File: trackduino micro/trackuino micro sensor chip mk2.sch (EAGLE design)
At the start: 40 parts, among them IC2 74AHC1G125DBV, SW1 SPST_TACT-KMR2, U1 ATMEGA168MLF, Y1 16MHZ

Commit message: updates
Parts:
- removed LED3, LED4: (no value), adafruit:LEDCHIP-LED0805
- removed SHT15: SHT1XSMD, SparkFun-Sensors:SHT1XSMD
- added PTT, VCC: (no value), adafruit:LEDCHIP-LED0805
- added SHT21: SHT21, sht21:SHT21
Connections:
- net 3V: now also SHT21.VDD; no longer SHT15.VDD
- net GND: now also PTT.C, SHT21.VSS, VCC.C; no longer LED3.C, LED4.C, SHT15.GND
- net N$27: now also PTT.A; no longer LED4.A
- net N$8: now also VCC.A; no longer LED3.A
- net SCL: now also SHT21.SCL; no longer SHT15.SCK
- net SDA: now also SHT21.SDA; no longer SHT15.DATA
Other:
- note added: "Sensors"
- moved on the sheet: BMP180, C1, C2, C3, C4, C5, C7, C8, C9, D1, IC2, JP1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

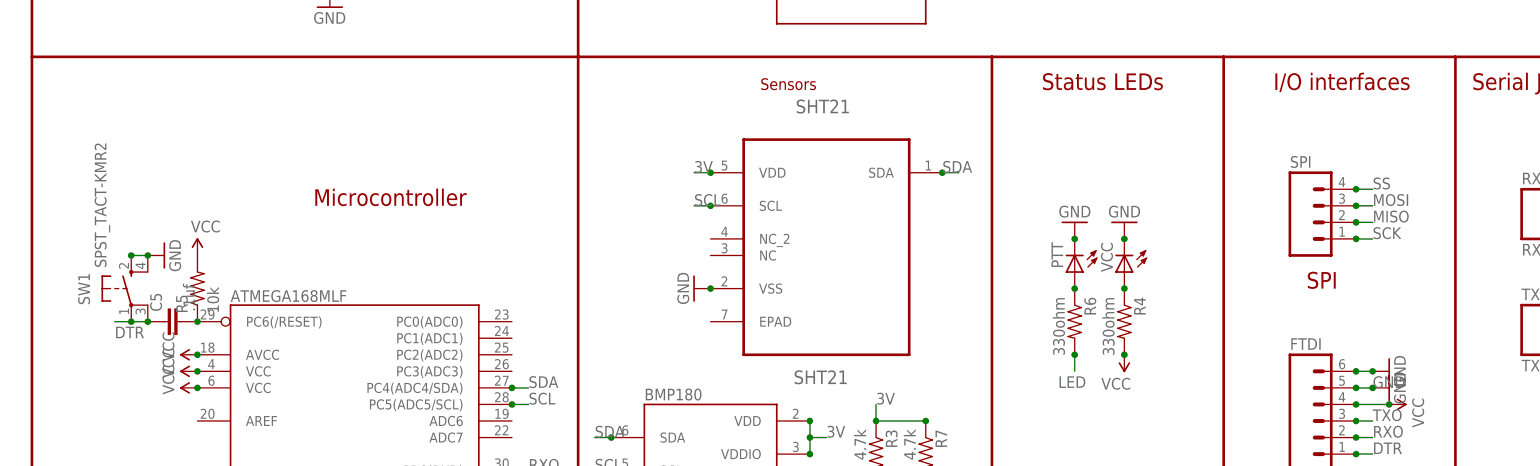
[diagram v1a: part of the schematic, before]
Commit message: added i2c breakout and fixed ftdi
added breakouts on all versions for i2c next to the spi header, replaced
IO breakout headers from .1" to 2mm to accomodate i2c.
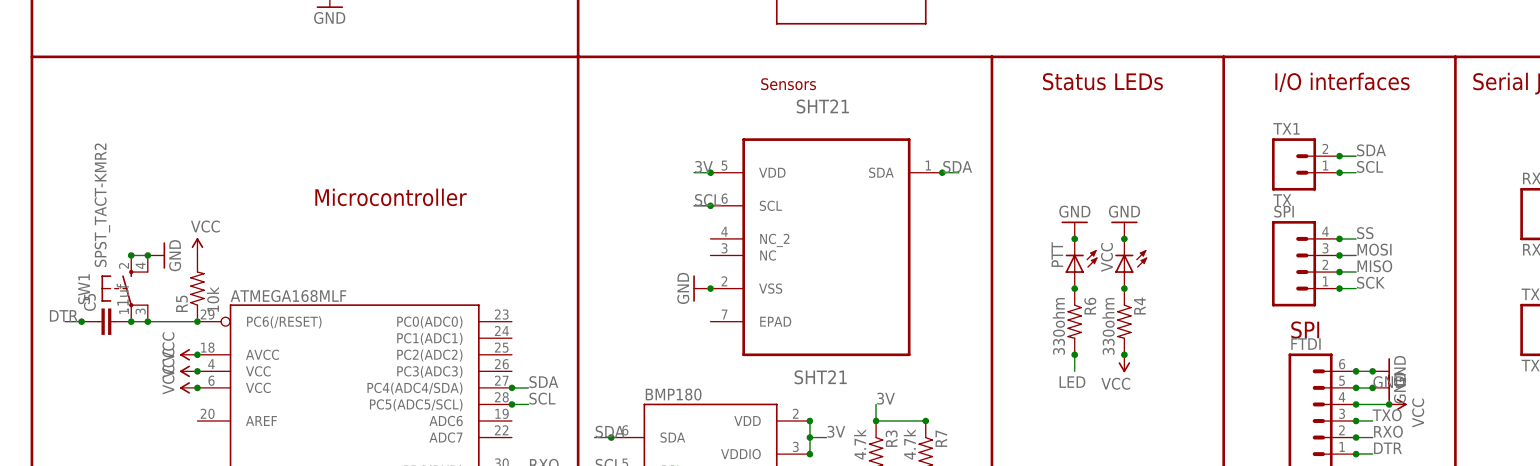
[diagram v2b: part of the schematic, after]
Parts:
- added TX1: TX, SparkFun-Connectors:M02JST-PTH-VERT
- SPI: device SparkFun-Connectors:M041X04_NO_SILK -> SparkFun-Connectors:M04JST-PTH-VERT
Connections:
- removed net N$7: C5.2, R5.1, U1.PC6(/RESET)
- new net N$17: C5.2, R5.1, SW1.P, SW1.P1, U1.PC6(/RESET)
- net DTR: no longer SW1.P, SW1.P1
- net SCL: now also TX1.1
- net SDA: now also TX1.2
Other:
- moved on the sheet: C5, SPI
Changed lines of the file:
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@@
 <part name="C5" library="SparkFun-Capacitors" deviceset="CAP" device="0805" value=".1uf"/>
 <part name="TX" library="SparkFun-Connectors" deviceset="M02" device="PTH" value="TX"/>
-<part name="SPI" library="SparkFun-Connectors" deviceset="M04" device="1X04_NO_SILK"/>
+<part name="SPI" library="SparkFun-Connectors" deviceset="M04" device="JST-PTH-VERT"/>
 <part name="GND23" library="SparkFun-Aesthetics" deviceset="GND" device=""/>
 <part name="FRAME1" library="SparkFun-Aesthetics" deviceset="FRAME-LETTER" device=""/>
@@
 <part name="SHT21" library="sht21" deviceset="SHT21" device=""/>
 <part name="U$3" library="SparkFun-RF" deviceset="ANTENNA2" device="SMD3"/>
+<part name="TX1" library="SparkFun-Connectors" deviceset="M02" device="JST-PTH-VERT" value="TX"/>
 </parts>
 <sheets>
@@
 <text x="190.5" y="104.14" size="2.54" layer="94">I/O interfaces</text>
 <text x="220.98" y="104.14" size="2.54" layer="94">Serial Jumpers</text>
-<text x="195.58" y="73.66" size="2.54" layer="94">SPI</text>
+<text x="193.04" y="66.04" size="2.54" layer="94">SPI</text>
 <text x="195.58" y="40.64" size="2.54" layer="94">FTDI</text>
 <wire x1="147.32" y1="35.56" x2="83.82" y2="35.56" width="0.1524" layer="94"/>
@@
 <instance part="R5" gate="G$1" x="25.4" y="73.66" rot="R90"/>
 <instance part="SUPPLY10" gate="G$1" x="25.4" y="78.74"/>
-<instance part="C5" gate="G$1" x="22.86" y="68.58" rot="R90"/>
+<instance part="C5" gate="G$1" x="12.7" y="68.58" rot="R90"/>
 <instance part="TX" gate="G$1" x="231.14" y="66.04"/>
-<instance part="SPI" gate="G$1" x="198.12" y="83.82"/>
+<instance part="SPI" gate="G$1" x="195.58" y="76.2"/>
 <instance part="GND23" gate="1" x="20.32" y="78.74" rot="R90"/>
 <instance part="FRAME1" gate="G$1" x="0" y="0"/>
@@
 <instance part="SHT21" gate="A" x="121.92" y="83.82"/>
 <instance part="U$3" gate="G$1" x="165.1" y="165.1" rot="R90"/>
+<instance part="TX1" gate="G$1" x="193.04" y="91.44"/>
 </instances>
 <busses>
@@
 </segment>
 <segment>
-<pinref part="SW1" gate="G$1" pin="P"/>
-<wire x1="15.24" y1="68.58" x2="17.78" y2="68.58" width="0.1524" layer="91"/>
-<pinref part="SW1" gate="G$1" pin="P1"/>
 <pinref part="C5" gate="G$1" pin="1"/>
-<junction x="17.78" y="68.58"/>
-<junction x="15.24" y="68.58"/>
-<wire x1="15.24" y1="68.58" x2="12.7" y2="68.58" width="0.1524" layer="91"/>
-<label x="12.7" y="66.04" size="1.778" layer="95"/>
+<wire x1="7.62" y1="68.58" x2="5.08" y2="68.58" width="0.1524" layer="91"/>
+<junction x="7.62" y="68.58"/>
+<label x="2.54" y="68.58" size="1.778" layer="95"/>
 </segment>
 </net>
@@
 <segment>
 <pinref part="SPI" gate="G$1" pin="2"/>
-<wire x1="203.2" y1="83.82" x2="205.74" y2="83.82" width="0.1524" layer="91"/>
-<label x="205.74" y="83.82" size="1.778" layer="95"/>
-<junction x="203.2" y="83.82"/>
+<wire x1="200.66" y1="76.2" x2="203.2" y2="76.2" width="0.1524" layer="91"/>
+<label x="203.2" y="76.2" size="1.778" layer="95"/>
+<junction x="200.66" y="76.2"/>
 </segment>
 </net>
@@
 <segment>
 <pinref part="SPI" gate="G$1" pin="3"/>
-<wire x1="203.2" y1="86.36" x2="205.74" y2="86.36" width="0.1524" layer="91"/>
-<label x="205.74" y="86.36" size="1.778" layer="95"/>
-<junction x="203.2" y="86.36"/>
+<wire x1="200.66" y1="78.74" x2="203.2" y2="78.74" width="0.1524" layer="91"/>
+<label x="203.2" y="78.74" size="1.778" layer="95"/>
+<junction x="200.66" y="78.74"/>
 </segment>
 </net>
@@
 <segment>
 <pinref part="SPI" gate="G$1" pin="1"/>
-<wire x1="203.2" y1="81.28" x2="205.74" y2="81.28" width="0.1524" layer="91"/>
-<label x="205.74" y="81.28" size="1.778" layer="95"/>
-<junction x="203.2" y="81.28"/>
+<wire x1="200.66" y1="73.66" x2="203.2" y2="73.66" width="0.1524" layer="91"/>
+<label x="203.2" y="73.66" size="1.778" layer="95"/>
+<junction x="200.66" y="73.66"/>
 </segment>
 </net>
@@
 <segment>
 <pinref part="SPI" gate="G$1" pin="4"/>
-<wire x1="203.2" y1="88.9" x2="205.74" y2="88.9" width="0.1524" layer="91"/>
-<label x="205.74" y="88.9" size="1.778" layer="95"/>
-<junction x="203.2" y="88.9"/>
+<wire x1="200.66" y1="81.28" x2="203.2" y2="81.28" width="0.1524" layer="91"/>
+<label x="203.2" y="81.28" size="1.778" layer="95"/>
+<junction x="200.66" y="81.28"/>
 </segment>
 </net>
@@
 <junction x="129.54" y="43.18"/>
 </segment>
+<segment>
+<pinref part="TX1" gate="G$1" pin="2"/>
+<wire x1="200.66" y1="93.98" x2="203.2" y2="93.98" width="0.1524" layer="91"/>
+<label x="203.2" y="93.98" size="1.778" layer="95"/>
+<junction x="200.66" y="93.98"/>
+</segment>
 </net>
 <net name="SCL" class="0">
@@
 <label x="137.16" y="40.64" size="1.778" layer="95"/>
 <junction x="137.16" y="43.18"/>
+</segment>
+<segment>
+<pinref part="TX1" gate="G$1" pin="1"/>
+<wire x1="200.66" y1="91.44" x2="203.2" y2="91.44" width="0.1524" layer="91"/>
+<label x="203.2" y="91.44" size="1.778" layer="95"/>
+<junction x="200.66" y="91.44"/>
 </segment>
 </net>
@@
 </segment>
 </net>
-<net name="N$7" class="0">
-<segment>
-<pinref part="U1" gate="G$1" pin="PC6(/RESET)"/>
-<pinref part="R5" gate="G$1" pin="1"/>
-<pinref part="C5" gate="G$1" pin="2"/>
-<junction x="25.4" y="68.58"/>
-<pinref part="C5" gate="G$1" pin="2"/>
-</segment>
-</net>
 <net name="N$9" class="0">
 <segment>
@@
 </segment>
 </net>
+<net name="N$17" class="0">
+<segment>
+<pinref part="C5" gate="G$1" pin="2"/>
+<pinref part="C5" gate="G$1" pin="2"/>
+<pinref part="SW1" gate="G$1" pin="P1"/>
+<wire x1="15.24" y1="68.58" x2="17.78" y2="68.58" width="0.1524" layer="91"/>
+<pinref part="U1" gate="G$1" pin="PC6(/RESET)"/>
+<pinref part="R5" gate="G$1" pin="1"/>
+<wire x1="17.78" y1="68.58" x2="25.4" y2="68.58" width="0.1524" layer="91"/>
+<pinref part="SW1" gate="G$1" pin="P"/>
+<junction x="15.24" y="68.58"/>
+<junction x="17.78" y="68.58"/>
+<junction x="25.4" y="68.58"/>
+</segment>
+</net>

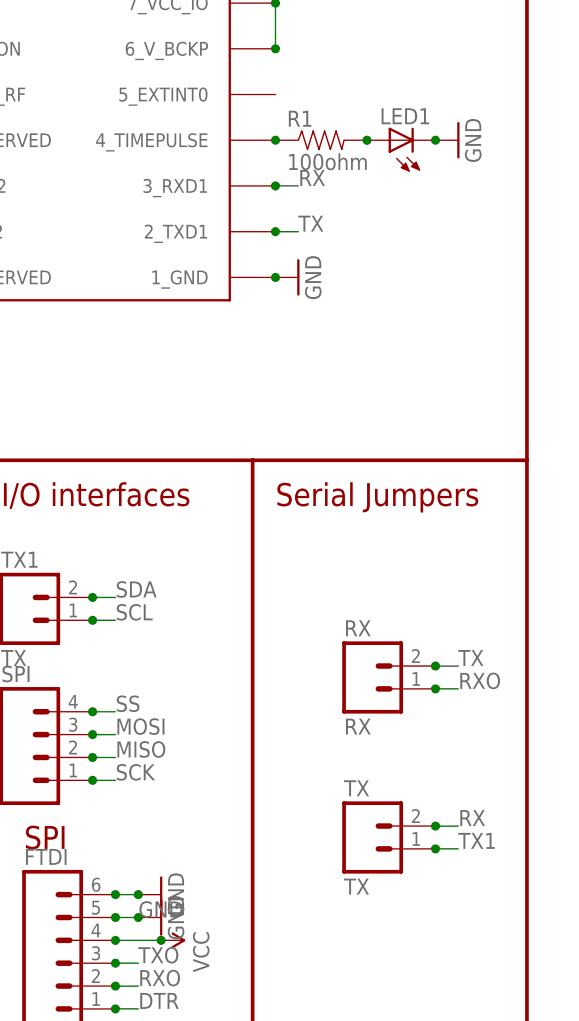
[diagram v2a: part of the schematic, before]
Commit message: fixed chip serial GPS connection
Serial connection between GPS and Avr chip was not wired correctly.
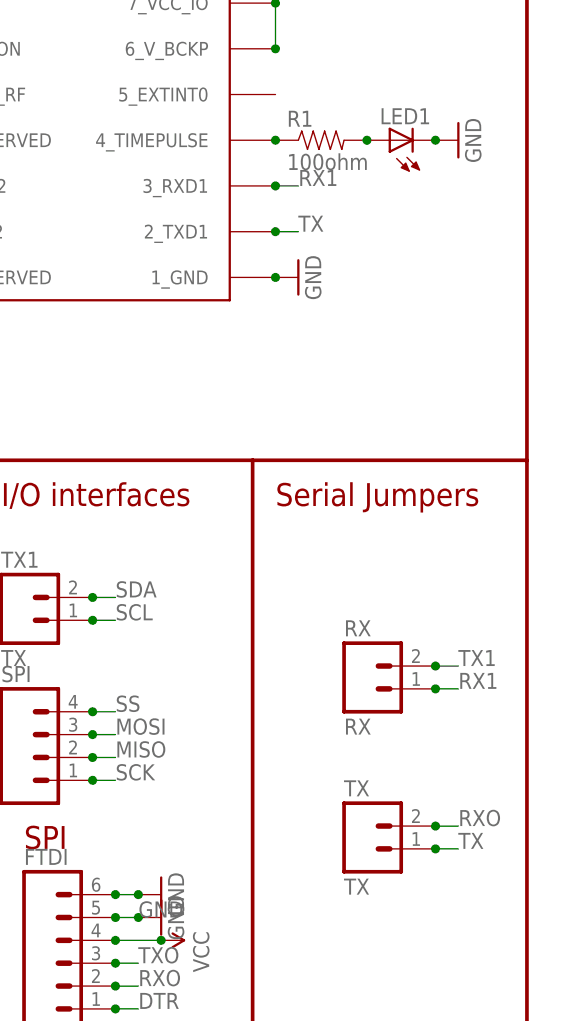
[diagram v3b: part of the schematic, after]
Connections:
- removed net RX: TX.2, U$1.3_RXD1
- new net RX1: RX.1, U$1.3_RXD1
- net RXO: now also TX.2; no longer RX.1
- net TX: now also TX.1; no longer RX.2
- net TX1: now also RX.2; no longer TX.1
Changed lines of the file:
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@@
-</segment>
-</net>
-<net name="TX" class="0">
-<segment>
-<wire x1="220.98" y1="134.62" x2="223.52" y2="134.62" width="0.1524" layer="91"/>
-<label x="223.52" y="134.62" size="1.778" layer="95"/>
-<pinref part="U$1" gate="G$1" pin="2_TXD1"/>
-<junction x="220.98" y="134.62"/>
-</segment>
-<segment>
-<pinref part="RX" gate="G$1" pin="2"/>
-<wire x1="238.76" y1="86.36" x2="241.3" y2="86.36" width="0.1524" layer="91"/>
-<label x="241.3" y="86.36" size="1.778" layer="95"/>
-<junction x="238.76" y="86.36"/>
 </segment>
 </net>
@@
 </segment>
 </net>
-<net name="RX" class="0">
-<segment>
-<wire x1="223.52" y1="139.7" x2="220.98" y2="139.7" width="0.1524" layer="91"/>
-<label x="223.52" y="139.7" size="1.778" layer="95"/>
-<pinref part="U$1" gate="G$1" pin="3_RXD1"/>
-<junction x="220.98" y="139.7"/>
+<net name="N$8" class="0">
+<segment>
+<pinref part="VCC" gate="G$1" pin="A"/>
+<pinref part="R4" gate="G$1" pin="1"/>
+<junction x="167.64" y="73.66"/>
+</segment>
+</net>
+<net name="DTR" class="0">
+<segment>
+<pinref part="FTDI" gate="G$1" pin="1"/>
+<wire x1="203.2" y1="48.26" x2="205.74" y2="48.26" width="0.1524" layer="91"/>
+<label x="205.74" y="48.26" size="1.778" layer="95"/>
+<junction x="203.2" y="48.26"/>
+</segment>
+<segment>
+<pinref part="C5" gate="G$1" pin="1"/>
+<wire x1="7.62" y1="68.58" x2="5.08" y2="68.58" width="0.1524" layer="91"/>
+<junction x="7.62" y="68.58"/>
+<label x="2.54" y="68.58" size="1.778" layer="95"/>
+</segment>
+</net>
+<net name="RXO" class="0">
+<segment>
+<pinref part="U1" gate="G$1" pin="PD0(RXD)"/>
+<wire x1="73.66" y1="45.72" x2="76.2" y2="45.72" width="0.1524" layer="91"/>
+<label x="76.2" y="45.72" size="1.778" layer="95"/>
+<junction x="73.66" y="45.72"/>
+</segment>
+<segment>
+<pinref part="FTDI" gate="G$1" pin="2"/>
+<wire x1="203.2" y1="50.8" x2="205.74" y2="50.8" width="0.1524" layer="91"/>
+<label x="205.74" y="50.8" size="1.778" layer="95"/>
+<junction x="203.2" y="50.8"/>
 </segment>
 <segment>
@@
 </segment>
 </net>
-<net name="N$8" class="0">
-<segment>
-<pinref part="VCC" gate="G$1" pin="A"/>
-<pinref part="R4" gate="G$1" pin="1"/>
-<junction x="167.64" y="73.66"/>
-</segment>
-</net>
-<net name="DTR" class="0">
-<segment>
-<pinref part="FTDI" gate="G$1" pin="1"/>
-<wire x1="203.2" y1="48.26" x2="205.74" y2="48.26" width="0.1524" layer="91"/>
-<label x="205.74" y="48.26" size="1.778" layer="95"/>
-<junction x="203.2" y="48.26"/>
-</segment>
-<segment>
-<pinref part="C5" gate="G$1" pin="1"/>
-<wire x1="7.62" y1="68.58" x2="5.08" y2="68.58" width="0.1524" layer="91"/>
-<junction x="7.62" y="68.58"/>
-<label x="2.54" y="68.58" size="1.778" layer="95"/>
-</segment>
-</net>
-<net name="RXO" class="0">
-<segment>
-<pinref part="U1" gate="G$1" pin="PD0(RXD)"/>
-<wire x1="73.66" y1="45.72" x2="76.2" y2="45.72" width="0.1524" layer="91"/>
-<label x="76.2" y="45.72" size="1.778" layer="95"/>
-<junction x="73.66" y="45.72"/>
-</segment>
-<segment>
-<pinref part="FTDI" gate="G$1" pin="2"/>
-<wire x1="203.2" y1="50.8" x2="205.74" y2="50.8" width="0.1524" layer="91"/>
-<label x="205.74" y="50.8" size="1.778" layer="95"/>
-<junction x="203.2" y="50.8"/>
-</segment>
-<segment>
-<pinref part="RX" gate="G$1" pin="1"/>
-<wire x1="238.76" y1="83.82" x2="241.3" y2="83.82" width="0.1524" layer="91"/>
-<label x="241.3" y="83.82" size="1.778" layer="95"/>
-<junction x="238.76" y="83.82"/>
-</segment>
-</net>
 <net name="TXO" class="0">
 <segment>
@@
 </segment>
 <segment>
-<pinref part="TX" gate="G$1" pin="1"/>
-<wire x1="238.76" y1="66.04" x2="241.3" y2="66.04" width="0.1524" layer="91"/>
-<label x="241.3" y="66.04" size="1.778" layer="95"/>
-<junction x="238.76" y="66.04"/>
+<pinref part="RX" gate="G$1" pin="2"/>
+<wire x1="238.76" y1="86.36" x2="241.3" y2="86.36" width="0.1524" layer="91"/>
+<label x="241.3" y="86.36" size="1.778" layer="95"/>
+<junction x="238.76" y="86.36"/>
 </segment>
 </net>
@@
 </segment>
 </net>
+<net name="RX1" class="0">
+<segment>
+<wire x1="223.52" y1="139.7" x2="220.98" y2="139.7" width="0.1524" layer="91"/>
+<label x="223.52" y="139.7" size="1.778" layer="95"/>
+<pinref part="U$1" gate="G$1" pin="3_RXD1"/>
+<junction x="220.98" y="139.7"/>
+</segment>
+<segment>
+<pinref part="RX" gate="G$1" pin="1"/>
+<wire x1="238.76" y1="83.82" x2="241.3" y2="83.82" width="0.1524" layer="91"/>
+<label x="241.3" y="83.82" size="1.778" layer="95"/>
+<junction x="238.76" y="83.82"/>
+</segment>
+</net>
+<net name="TX" class="0">
+<segment>
+<wire x1="220.98" y1="134.62" x2="223.52" y2="134.62" width="0.1524" layer="91"/>
+<label x="223.52" y="134.62" size="1.778" layer="95"/>
+<pinref part="U$1" gate="G$1" pin="2_TXD1"/>
+<junction x="220.98" y="134.62"/>
+</segment>
+<segment>
+<pinref part="TX" gate="G$1" pin="1"/>
+<wire x1="238.76" y1="66.04" x2="241.3" y2="66.04" width="0.1524" layer="91"/>
+<label x="241.3" y="66.04" size="1.778" layer="95"/>
+<junction x="238.76" y="66.04"/>
+</segment>
+</net>
